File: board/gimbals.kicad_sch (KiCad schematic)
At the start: 4 parts

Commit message: Added most Footprints, Schematic review touch up
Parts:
- Conn5, Conn6, Conn7, Conn8: footprint (none) -> MRDT_Connectors:MOLEX_SL_04_Vertical
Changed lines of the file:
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@@
 			)
 		)
-		(property "Footprint" ""
+		(property "Footprint" "MRDT_Connectors:MOLEX_SL_04_Vertical"
 			(at 97.79 53.34 0)
 			(effects
@@
 			)
 		)
-		(property "Footprint" ""
+		(property "Footprint" "MRDT_Connectors:MOLEX_SL_04_Vertical"
 			(at 48.26 53.34 0)
 			(effects
@@
 			)
 		)
-		(property "Footprint" ""
+		(property "Footprint" "MRDT_Connectors:MOLEX_SL_04_Vertical"
 			(at 148.59 53.34 0)
 			(effects
@@
 			)
 		)
-		(property "Footprint" ""
+		(property "Footprint" "MRDT_Connectors:MOLEX_SL_04_Vertical"
 			(at 200.66 53.34 0)
 			(effects

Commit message: Preliminary changes for rev2
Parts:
- added C4: 7.5µF, Capacitor_SMD:C_0603_1608Metric_Pad1.08x0.95mm_HandSolder, symbol Device:C
- added D21: 1N4148WT, Diode_SMD:D_SOD-523, symbol Diode:1N4148WT
- added L1: 500mH, symbol Device:L
- added Q11: BSS138, Package_TO_SOT_SMD:SOT-23, symbol Transistor_FET:BSS138
- added R17: 2500, Resistor_SMD:R_0603_1608Metric_Pad0.98x0.95mm_HandSolder, symbol Device:R_US
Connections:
- net GND: now also C4.2, D21.2 (A), R17.2
- new net: C4.1, L1.2, R17.1
- new net: D21.1 (K), L1.1, Q11.2 (S)
- new net +12V: Q11.3 (D)
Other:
- moved on the sheet: Conn7

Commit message: rev2 progress
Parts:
- removed C4: 7.5µF, Capacitor_SMD:C_0603_1608Metric_Pad1.08x0.95mm_HandSolder, symbol Device:C
- removed D21: 1N4148WT, Diode_SMD:D_SOD-523, symbol Diode:1N4148WT
- removed L1: 500mH, symbol Device:L
- removed Q11: BSS138, Package_TO_SOT_SMD:SOT-23, symbol Transistor_FET:BSS138
- removed R17: 2500, Resistor_SMD:R_0603_1608Metric_Pad0.98x0.95mm_HandSolder, symbol Device:R_US

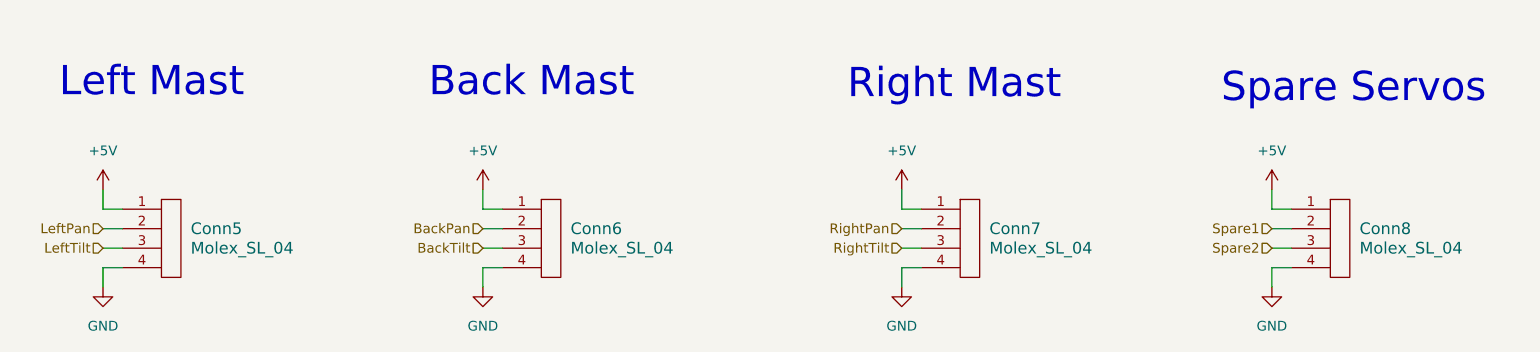
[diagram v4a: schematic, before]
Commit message: add voltage selection jumpers on servos
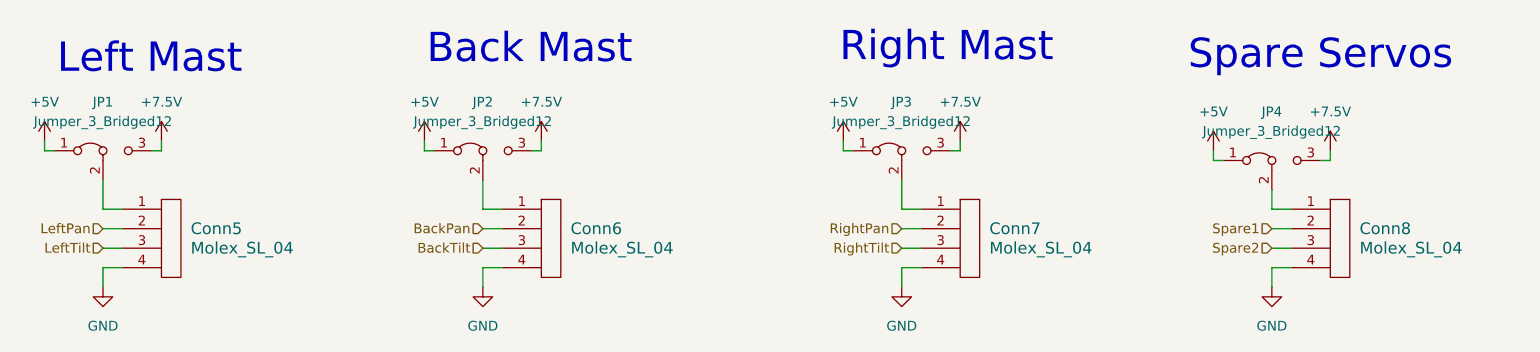
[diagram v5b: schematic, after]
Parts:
- added JP1, JP2, JP3, JP4: Jumper_3_Bridged12, Connector_PinHeader_2.54mm:PinHeader_1x03_P2.54mm_Vertical, symbol Jumper:Jumper_3_Bridged12
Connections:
- net +5V: now also JP1.1 (A), JP2.1 (A), JP3.1 (A), JP4.1 (A); no longer Conn5.1, Conn6.1, Conn7.1, Conn8.1
- new net: Conn6.1, JP2.2 (C)
- new net: Conn5.1, JP1.2 (C)
- new net: Conn8.1, JP4.2 (C)
- new net: Conn7.1, JP3.2 (C)
- new net +7.5V: JP1.3 (B), JP2.3 (B), JP3.3 (B), JP4.3 (B)
